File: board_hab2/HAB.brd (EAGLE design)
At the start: 127.1 x 103 mm, 39 parts, among them Q1 2N5496, Q2 2N5496, T2 2N3904

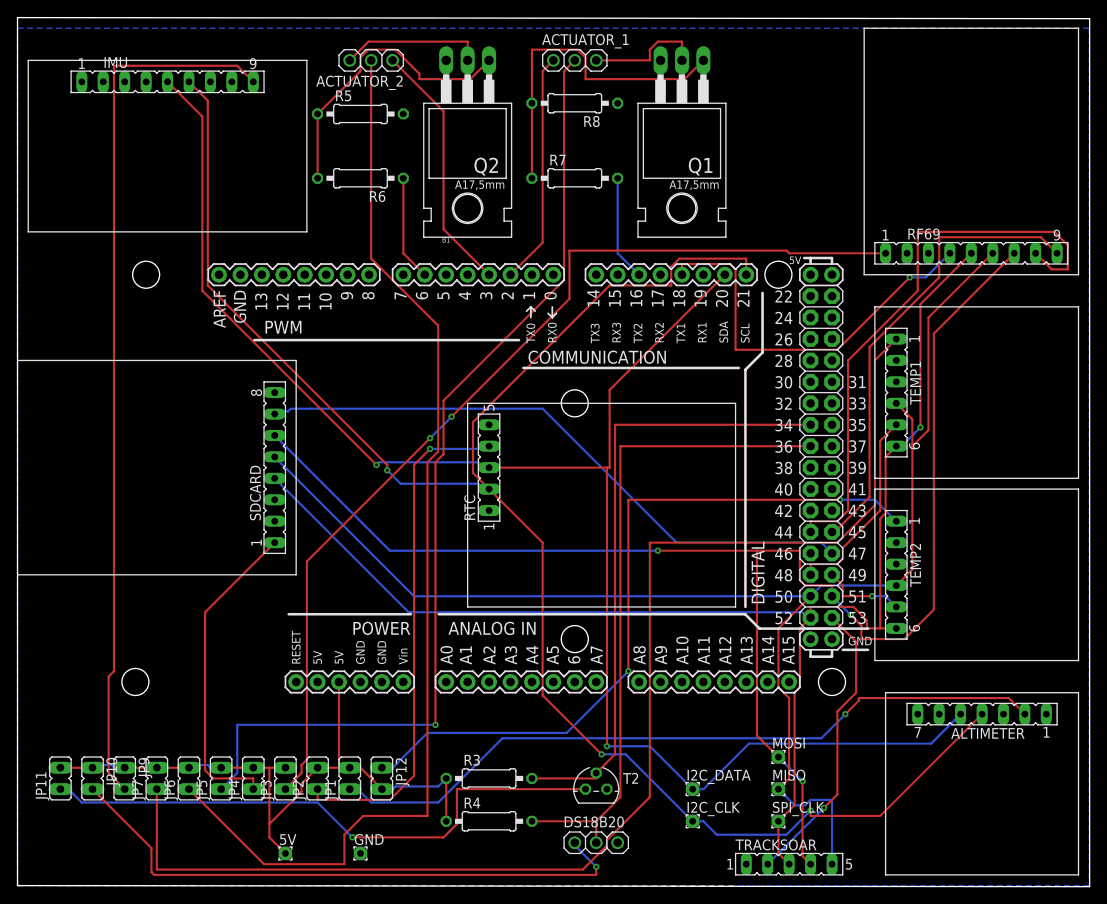
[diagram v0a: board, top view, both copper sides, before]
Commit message: Added gerbers and updated thick trace
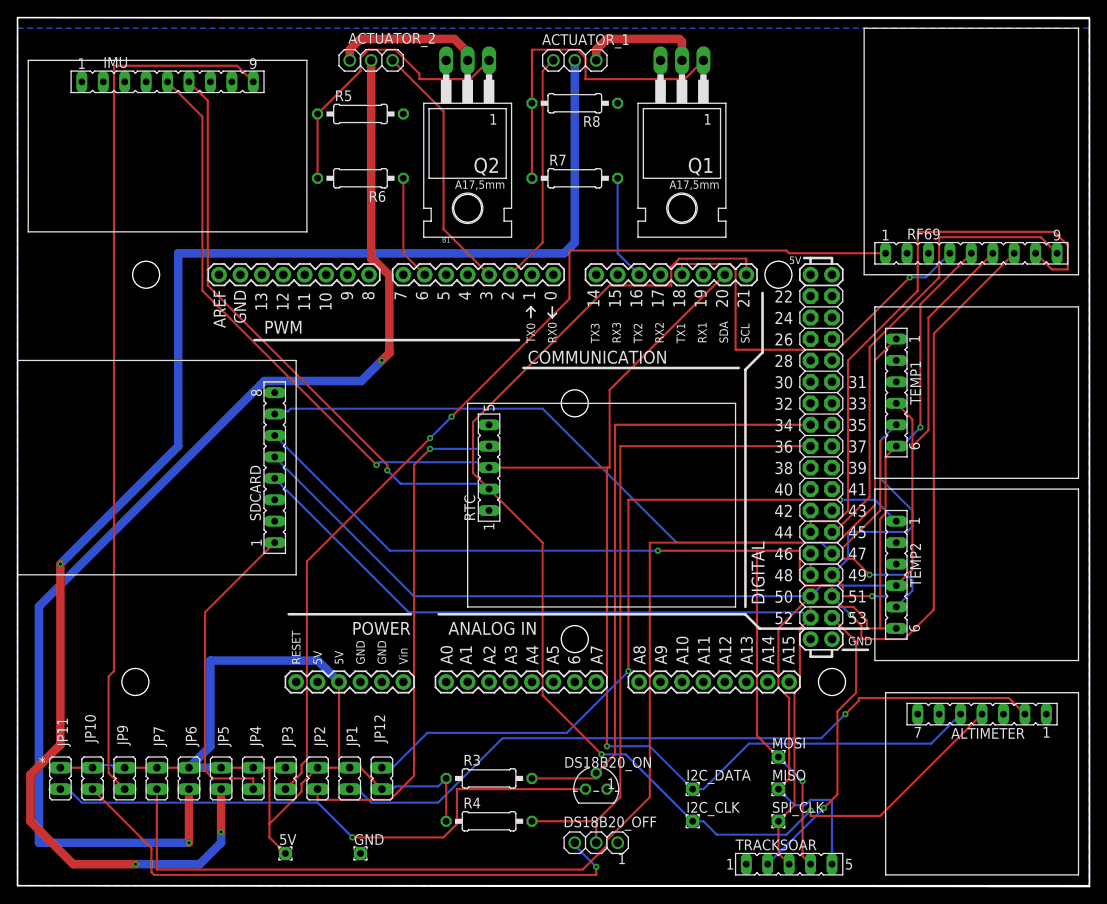
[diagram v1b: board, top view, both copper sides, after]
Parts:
- renumbered DS18B20 to DS18B20_OFF
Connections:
- net CS_T1: now also TEMP1.5; no longer TEMP2.5
- net CS_T2: now also TEMP2.5; no longer TEMP1.5
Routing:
- net N$16: track 117.5 -> 175.8 mm, vias 1 -> 3
- net VCC: track 79.2 -> 109.0 mm
- net CS_T1: track 9.94 -> 36.3 mm
- net N$17: track 129.7 -> 141.8 mm, vias 0 -> 2
- net CS_T2: track 23.8 -> 34.4 mm, vias 0 -> 1
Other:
- outline, holes or cut-outs redrawn
- board text added: "*"
- board text added: "1"
- board text added: "DS18B20_ON"
